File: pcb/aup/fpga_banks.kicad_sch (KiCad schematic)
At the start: 1 part, among them U1 XC7A50T-FGG484

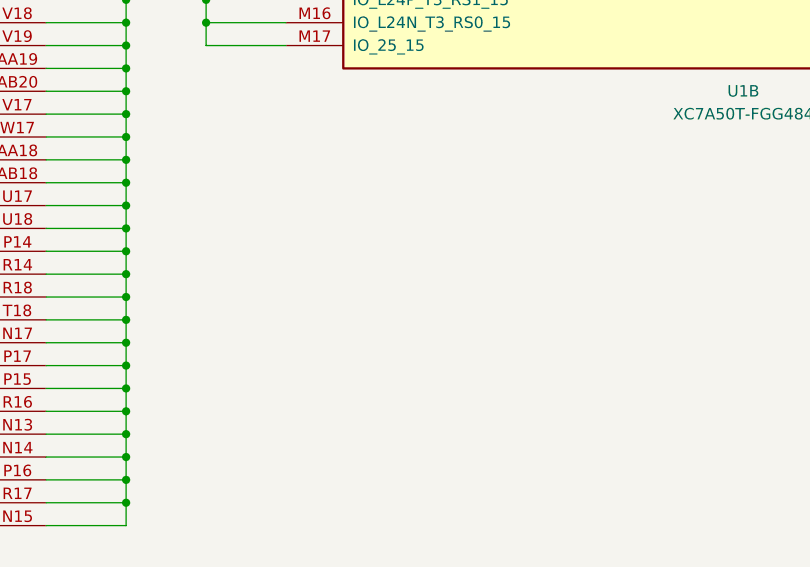
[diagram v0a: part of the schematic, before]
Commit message: Various explorations of layout
The pcb file is a mess with options. Saving this in a branch
to revisit it after interim layout.
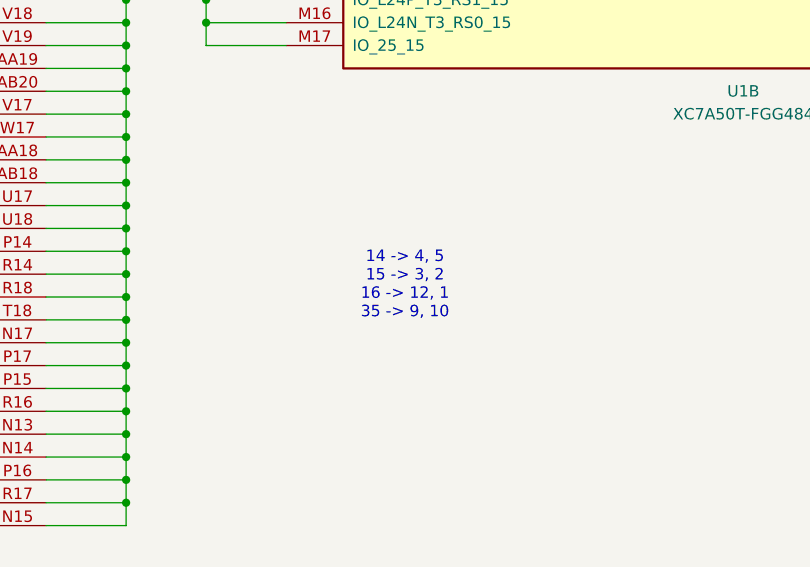
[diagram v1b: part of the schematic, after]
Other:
- note added: "14 -> 4, 5 15 -> 3, 2 16 -> 12, 1 35 -> 9, 10"
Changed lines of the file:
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@@
 	(generator_version "9.0")
 	(paper "USLedger")
+	(text "14 -> 4, 5\n15 -> 3, 2\n16 -> 12, 1\n35 -> 9, 10"
+		(exclude_from_sim no)
+		(at 163.068 233.68 0)
+		(effects
+			(font
+				(size 1.27 1.27)
+			)
+		)
+	)
 	(junction
 		(at 140.97 140.97)
@@
 		(polyline
 			(pts
-				(xy 124.46 133.35) (xy 124.46 262.89) (xy 127 262.89) (xy 127 133.35)
+				(xy 143.51 81.28) (xy 143.51 210.82) (xy 146.05 210.82) (xy 146.05 81.28)
 			)
 			(stroke
@@
 		(polyline
 			(pts
-				(xy 143.51 81.28) (xy 143.51 210.82) (xy 146.05 210.82) (xy 146.05 81.28)
+				(xy 124.46 133.35) (xy 124.46 262.89) (xy 127 262.89) (xy 127 133.35)
 			)
 			(stroke

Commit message: Switch to QSH-60
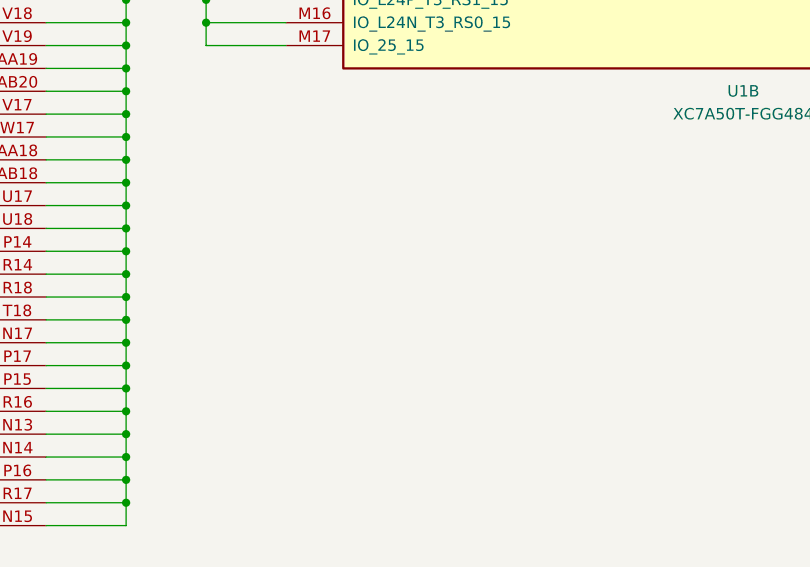
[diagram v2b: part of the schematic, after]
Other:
- note removed: "14 -> 4, 5 15 -> 3, 2 16 -> 12, 1 35 -> 9, 10"
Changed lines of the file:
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@@
 	(generator_version "9.0")
 	(paper "USLedger")
-	(text "14 -> 4, 5\n15 -> 3, 2\n16 -> 12, 1\n35 -> 9, 10"
-		(exclude_from_sim no)
-		(at 163.068 233.68 0)
-		(effects
-			(font
-				(size 1.27 1.27)
-			)
-		)
-	)
 	(junction
 		(at 140.97 140.97)
@@
 		(polyline
 			(pts
-				(xy 26.67 24.13) (xy 26.67 67.31) (xy 29.21 67.31) (xy 29.21 24.13)
+				(xy 143.51 81.28) (xy 143.51 210.82) (xy 146.05 210.82) (xy 146.05 81.28)
 			)
 			(stroke
@@
 		(polyline
 			(pts
-				(xy 143.51 81.28) (xy 143.51 210.82) (xy 146.05 210.82) (xy 146.05 81.28)
+				(xy 26.67 24.13) (xy 26.67 67.31) (xy 29.21 67.31) (xy 29.21 24.13)
 			)
 			(stroke
@@
 		(polyline
 			(pts
-				(xy 124.46 133.35) (xy 124.46 262.89) (xy 127 262.89) (xy 127 133.35)
+				(xy 402.59 92.71) (xy 402.59 222.25) (xy 405.13 222.25) (xy 405.13 92.71)
 			)
 			(stroke
@@
 		(polyline
 			(pts
-				(xy 402.59 92.71) (xy 402.59 222.25) (xy 405.13 222.25) (xy 405.13 92.71)
+				(xy 252.73 81.28) (xy 252.73 210.82) (xy 255.27 210.82) (xy 255.27 81.28)
 			)
 			(stroke
@@
 		(polyline
 			(pts
-				(xy 252.73 81.28) (xy 252.73 210.82) (xy 255.27 210.82) (xy 255.27 81.28)
+				(xy 124.46 133.35) (xy 124.46 262.89) (xy 127 262.89) (xy 127 133.35)
 			)
 			(stroke
